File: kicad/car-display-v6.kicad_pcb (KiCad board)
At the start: 4 copper layers, 35.8 x 35.8 mm, 43 parts, among them J1 AVR-ISP-10, J2 Screw_Terminal_01x03, J3 PicoBlade F 1x7, J4 Socket 1x6 0.1", U1 ATmega328PB-M, U2 MCP25625T-E/ML, U3 3.3V, U4 TPSM365R15FRDNR, U5 TPS3422, Y1 16MHZ

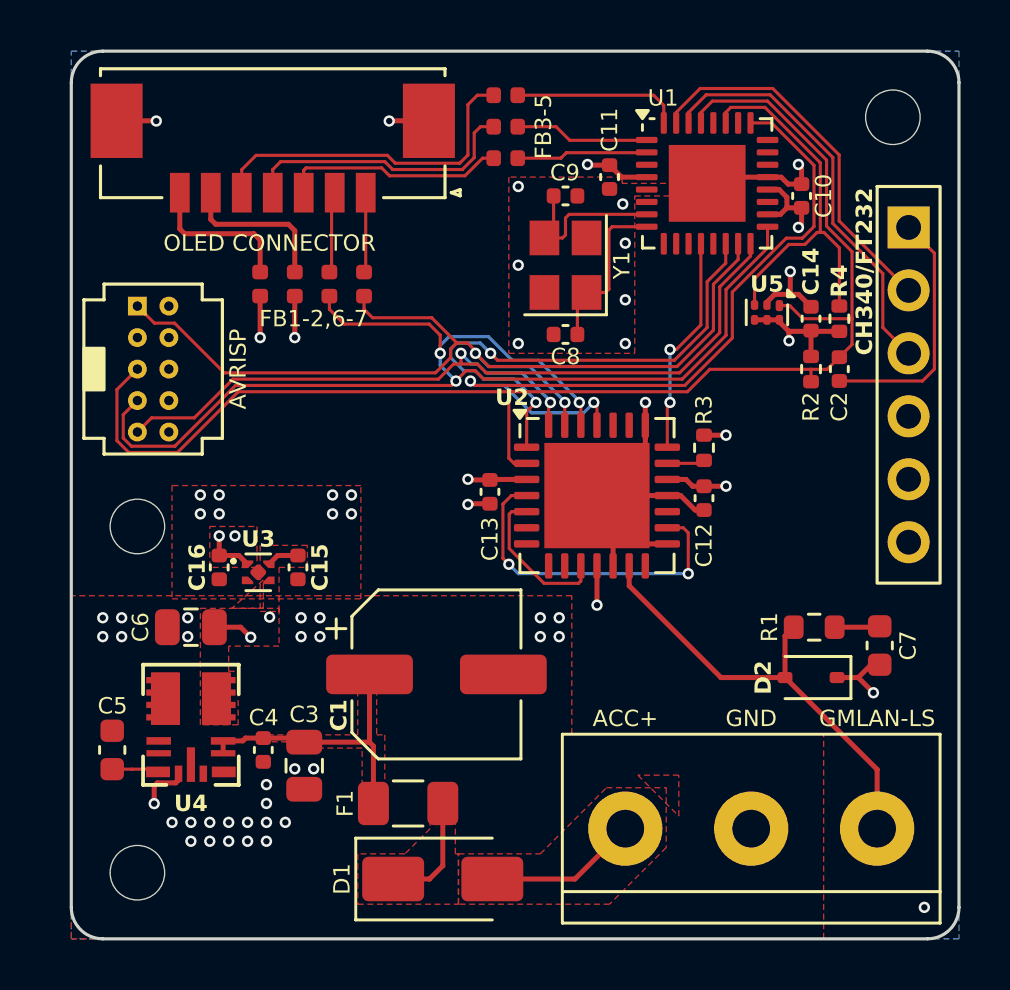
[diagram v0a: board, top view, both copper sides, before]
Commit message: Update PCB connectors
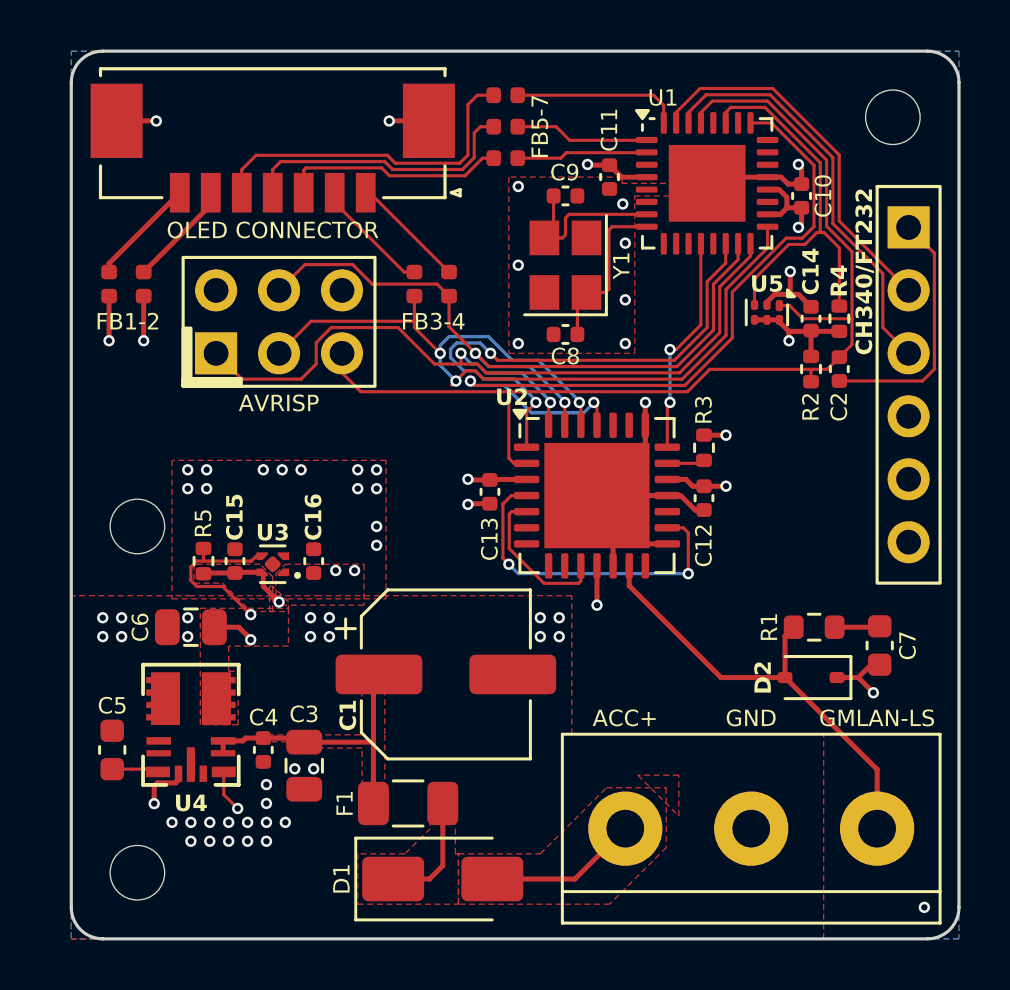
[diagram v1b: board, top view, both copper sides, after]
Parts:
- added R5: 10K, Resistor_SMD:R_0402_1005Metric, F.Cu at (81.5, 173.0)
- J1: value AVR-ISP-10 -> AVR-ISP-6; footprint jsdev:PinHeader_SWD_BD120-10-A-0305-0229-L-B -> jsdev:PinHeader_ISP_POGO
- U4: value TPSM365R15FRDNR -> 5V
- moved FB2 6.10 mm to (79.1, 161.8)
- moved FB1 6.10 mm to (77.7, 161.8)
- moved C16 3.82 mm to (86.0, 173.0), turned to 90 degrees
- moved FB3 3.43 mm to (90.0, 161.8)
- moved FB4 3.43 mm to (91.4, 161.8)
- moved J1 2.62 mm to (82.0, 164.6), turned to 90 degrees
- moved C15 2.55 mm to (82.8, 173.0), turned to 90 degrees
- moved U3 0.67 mm to (84.3, 173.1), turned to 180 degrees
- moved C1 0.38 mm to (91.3, 177.5)
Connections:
- J1 pad 1: MOSI -> MISO
- J1 pad 3: unconnected-(J1-NC-Pad3) -> SCK
- J1 pad 4: GND -> MOSI
- U1 pad 13: UNIT_SENSE -> unconnected-(U1-PB1-Pad13)
- U1 pad 26: SEL_UNIT -> unconnected-(U1-PC3-Pad26)
- U3 pad 3: +5V -> PGOOD
- U4 pad 1: unconnected-(U4-PGOOD-Pad1) -> PGOOD
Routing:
- net PGOOD: track 0.00 -> 17.3 mm, vias 0 -> 2
- net SCK: track 49.1 -> 35.6 mm
- net RESET: track 56.6 -> 44.1 mm
- net MOSI: track 40.2 -> 30.3 mm
- net /3F_GND: track 6.33 -> 4.32 mm
- net +3.3V: track 19.1 -> 17.1 mm
- net MISO: track 35.6 -> 33.6 mm
- net +5V: track 38.3 -> 40.2 mm
- net /3F_3.3V: track 6.18 -> 4.38 mm
- net /3F_MOSI: track 3.11 -> 4.69 mm
- net /3F_SCK: track 3.29 -> 4.78 mm
- net GND: track 33.5 -> 33.7 mm, vias 55 -> 60
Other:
- board text added: "FB1-2"
- board text added: "FB3-4"
- board text added: "FB5-7"
- board text removed: "FB1-2,6-7"
- board text removed: "FB3-5"

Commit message: Move some pins around
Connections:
- U1 pad 11: unconnected-(U1-PD7-Pad11) -> CS_CAN
- U1 pad 14: CS_CAN -> unconnected-(U1-PB2-Pad14)
- U1 pad 26: unconnected-(U1-PC3-Pad26) -> SW_RESET
- U1 pad 27: SW_RESET -> unconnected-(U1-PC4-Pad27)
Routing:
- net CS_CAN: track 21.5 -> 20.7 mm

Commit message: PCB updates
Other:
- board text added: "DISPLAY ADAPTER J-S.DEV"
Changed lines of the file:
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@@
+		)
+	)
+	(gr_text "DISPLAY ADAPTER  J-S.DEV"
+		(at 84.582 168.656 0)
+		(layer "F.SilkS")
+		(effects
+			(font
+				(size 0.762 0.762)
+				(thickness 0.127)
+			)
+			(justify bottom)
 		)
 	)

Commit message: Production cleanup
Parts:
- R4, R5: value 10K -> 100K
